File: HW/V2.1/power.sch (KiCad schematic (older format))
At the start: 67 parts, among them IC2 MIC4416, IC3 MIC4416, Q2 NTMS4816NR2G, Q3 NTMS4816NR2G, U4 LM358

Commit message: updated values
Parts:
- R35, R38: value 22 -> 5
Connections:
- net GND: now also R37.2
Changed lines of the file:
@@
 L power:GND #GND0139
 U 1 1 5D2B57D0
-P 2850 3150
-F 0 "#GND0139" H 2938 3143 20  0000 L CNN
-F 1 "GND" H 2938 3091 30  0000 L CNN
-F 2 "" H 2850 3150 70  0000 C CNN
-F 3 "" H 2850 3150 70  0000 C CNN
-	1    2850 3150
+P 2850 3100
+F 0 "#GND0139" H 2938 3093 20  0000 L CNN
+F 1 "GND" H 2938 3041 30  0000 L CNN
+F 2 "" H 2850 3100 70  0000 C CNN
+F 3 "" H 2850 3100 70  0000 C CNN
+	1    2850 3100
 	1    0    0    -1
 $EndComp
@@
 P 4400 2300
 F 0 "R35" V 4171 2300 60  0000 C CNN
-F 1 "22" V 4277 2300 60  0000 C CNN
+F 1 "5" V 4277 2300 60  0000 C CNN
 F 2 "Resistor_SMD:R_0603_1608Metric" H 4400 2060 60  0001 C CNN
 F 3 "" H 4400 2060 60  0000 C CNN
@@
 P 4500 4550
 F 0 "R38" V 4271 4550 60  0000 C CNN
-F 1 "22" V 4377 4550 60  0000 C CNN
+F 1 "5" V 4377 4550 60  0000 C CNN
 F 2 "Resistor_SMD:R_0603_1608Metric" H 4500 4310 60  0001 C CNN
 F 3 "" H 4500 4310 60  0000 C CNN
@@
 	2250 1850 2050 1850
 Wire Wire Line
-	2850 3000 2850 3150
+	2850 2950 2850 3100
 Wire Wire Line
 	2850 2650 2850 2600

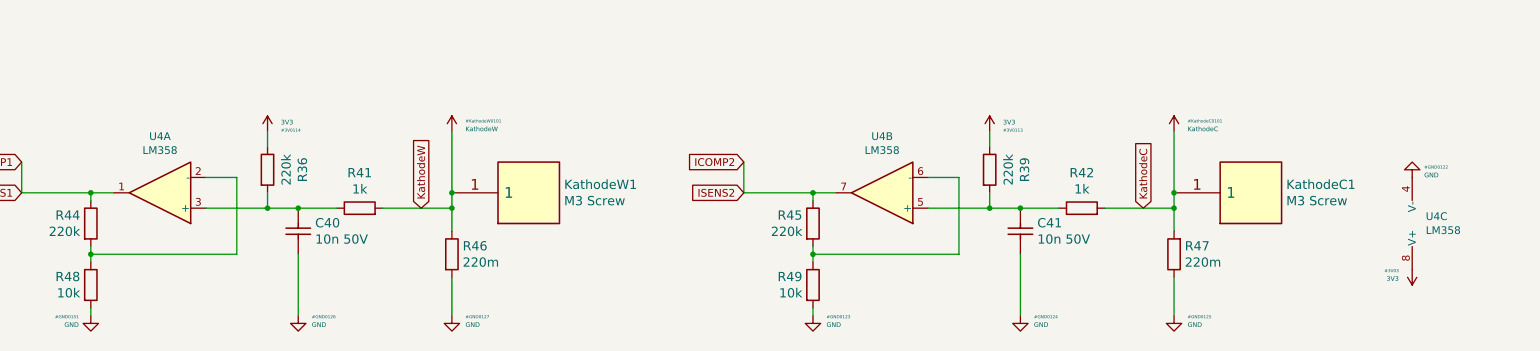
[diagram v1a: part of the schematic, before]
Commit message: fixed opamp
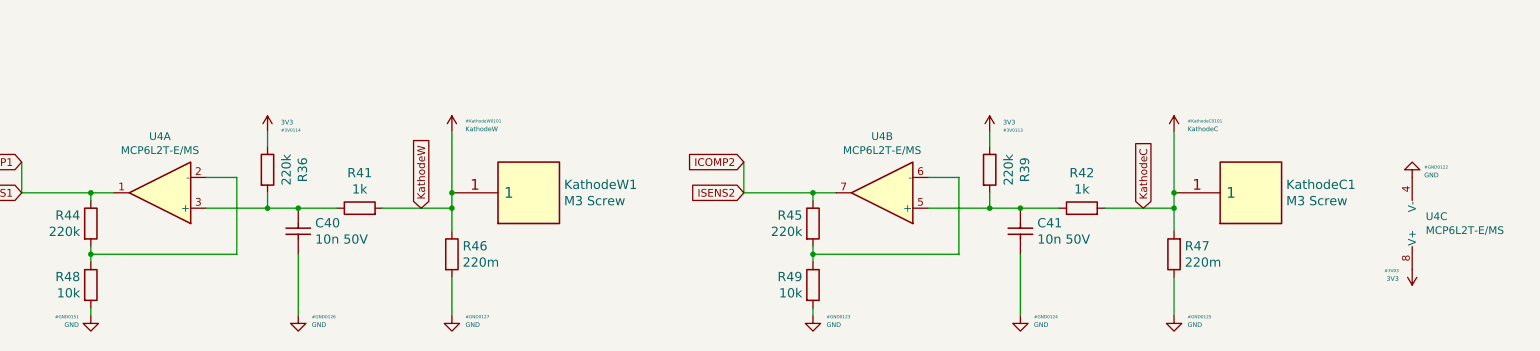
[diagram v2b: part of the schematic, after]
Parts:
- U4: value LM358 -> MCP6L2T-E/MS
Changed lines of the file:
@@
 P 5950 7900
 F 0 "U4" H 5950 7533 50  0000 C CNN
-F 1 "LM358" H 5950 7624 50  0000 C CNN
+F 1 "MCP6L2T-E/MS" H 5950 7624 50  0000 C CNN
 F 2 "Package_SO:MSOP-8_3x3mm_P0.65mm" H 5950 7900 50  0001 C CNN
 F 3 "http://www.ti.com/lit/ds/symlink/lm2904-n.pdf" H 5950 7900 50  0001 C CNN
@@
 P 10650 7900
 F 0 "U4" H 10650 7533 50  0000 C CNN
-F 1 "LM358" H 10650 7624 50  0000 C CNN
+F 1 "MCP6L2T-E/MS" H 10650 7624 50  0000 C CNN
 F 2 "Package_SO:MSOP-8_3x3mm_P0.65mm" H 10650 7900 50  0001 C CNN
 F 3 "http://www.ti.com/lit/ds/symlink/lm2904-n.pdf" H 10650 7900 50  0001 C CNN
@@
 P 14000 8100
 F 0 "U4" H 13812 8054 50  0000 R CNN
-F 1 "LM358" H 13812 8145 50  0000 R CNN
+F 1 "MCP6L2T-E/MS" H 13812 8145 50  0000 R CNN
 F 2 "Package_SO:MSOP-8_3x3mm_P0.65mm" H 14000 8100 50  0001 C CNN
 F 3 "http://www.ti.com/lit/ds/symlink/lm2904-n.pdf" H 14000 8100 50  0001 C CNN

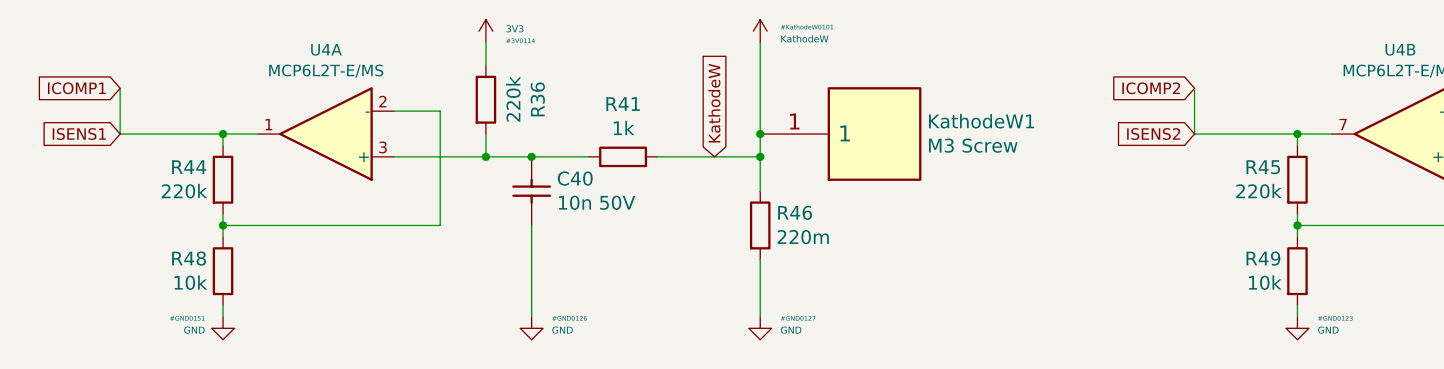
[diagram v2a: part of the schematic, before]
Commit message: fixed voltage divider for current measurement
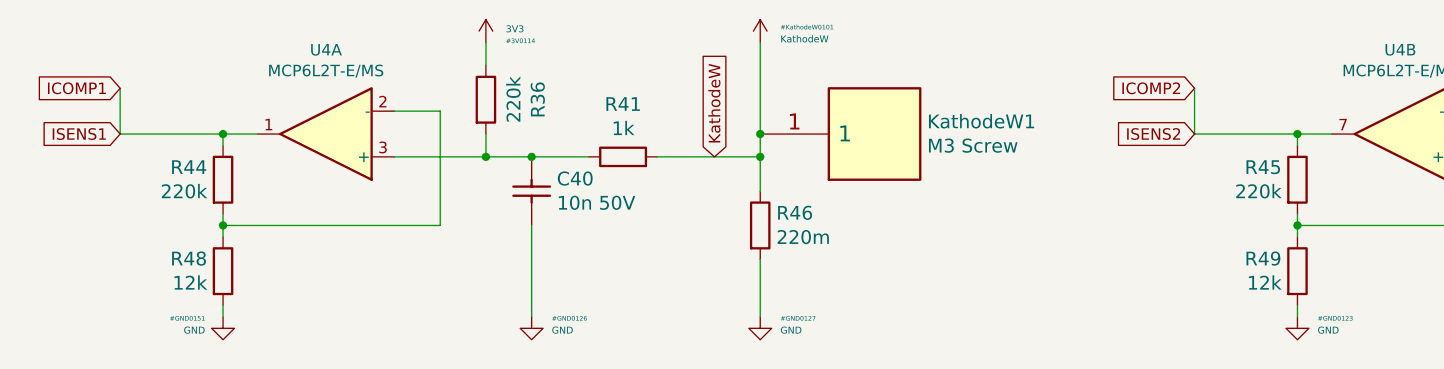
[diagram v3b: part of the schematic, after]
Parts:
- R48, R49: value 10k -> 12k
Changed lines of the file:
@@
 P 10200 8500
 F 0 "R49" H 10131 8553 60  0000 R CNN
-F 1 "10k" H 10131 8447 60  0000 R CNN
+F 1 "12k" H 10131 8447 60  0000 R CNN
 F 2 "Resistor_SMD:R_0603_1608Metric" H 10200 8360 60  0001 C CNN
 F 3 "" H 10200 8360 60  0000 C CNN
@@
 P 5500 8500
 F 0 "R48" H 5431 8553 60  0000 R CNN
-F 1 "10k" H 5431 8447 60  0000 R CNN
+F 1 "12k" H 5431 8447 60  0000 R CNN
 F 2 "Resistor_SMD:R_0603_1608Metric" H 5500 8360 60  0001 C CNN
 F 3 "" H 5500 8360 60  0000 C CNN

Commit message: added touch ic, fixed sk6812
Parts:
- LED1, LED2, LED3, LED4, LED5, LED9: footprint LED_SMD:LED_SK6812MINI_PLCC4_3.5x3.5mm_P1.75mm -> otter:sk6812mini
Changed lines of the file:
@@
 F 0 "LED1" H 12650 2939 60  0000 C CNN
 F 1 "SK6812" H 12650 2833 60  0000 C CNN
-F 2 "LED_SMD:LED_SK6812MINI_PLCC4_3.5x3.5mm_P1.75mm" H 12250 2050 60  0001 C CNN
+F 2 "otter:sk6812mini" H 12250 2050 60  0001 C CNN
 F 3 "" H 12250 2050 60  0000 C CNN
 	1    12650 2450
@@
 F 0 "LED2" H 12650 3789 60  0000 C CNN
 F 1 "SK6812" H 12650 3683 60  0000 C CNN
-F 2 "LED_SMD:LED_SK6812MINI_PLCC4_3.5x3.5mm_P1.75mm" H 12250 2900 60  0001 C CNN
+F 2 "otter:sk6812mini" H 12250 2900 60  0001 C CNN
 F 3 "" H 12250 2900 60  0000 C CNN
 	1    12650 3300
@@
 F 0 "LED3" H 12650 4639 60  0000 C CNN
 F 1 "SK6812" H 12650 4533 60  0000 C CNN
-F 2 "LED_SMD:LED_SK6812MINI_PLCC4_3.5x3.5mm_P1.75mm" H 12250 3750 60  0001 C CNN
+F 2 "otter:sk6812mini" H 12250 3750 60  0001 C CNN
 F 3 "" H 12250 3750 60  0000 C CNN
 	1    12650 4150
@@
 F 0 "LED4" H 12650 5489 60  0000 C CNN
 F 1 "SK6812" H 12650 5383 60  0000 C CNN
-F 2 "LED_SMD:LED_SK6812MINI_PLCC4_3.5x3.5mm_P1.75mm" H 12250 4600 60  0001 C CNN
+F 2 "otter:sk6812mini" H 12250 4600 60  0001 C CNN
 F 3 "" H 12250 4600 60  0000 C CNN
 	1    12650 5000
@@
 F 0 "LED5" H 12650 6300 60  0000 C CNN
 F 1 "SK6812" H 12650 6200 60  0000 C CNN
-F 2 "LED_SMD:LED_SK6812MINI_PLCC4_3.5x3.5mm_P1.75mm" H 12250 5450 60  0001 C CNN
+F 2 "otter:sk6812mini" H 12250 5450 60  0001 C CNN
 F 3 "" H 12250 5450 60  0000 C CNN
 	1    12650 5850
@@
 F 0 "LED9" H 12650 2089 60  0000 C CNN
 F 1 "SK6812" H 12650 1983 60  0000 C CNN
-F 2 "LED_SMD:LED_SK6812MINI_PLCC4_3.5x3.5mm_P1.75mm" H 12250 1200 60  0001 C CNN
+F 2 "otter:sk6812mini" H 12250 1200 60  0001 C CNN
 F 3 "" H 12250 1200 60  0000 C CNN
 	1    12650 1600
